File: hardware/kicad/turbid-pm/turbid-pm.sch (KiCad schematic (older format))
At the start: 12 parts, among them J1 Raspbery Pi, J2 PMS 7003, J3 Turbidity sensor, J4 Temp sensor A, J5 Temp sensor B

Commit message: new firmware and docs
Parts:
- removed J5: Temp sensor B, Connector_PinSocket_2.54mm:PinSocket_1x03_P2.54mm_Vertical, symbol Connector:Conn_01x03_Female
- removed R5: 4.7K, Resistor_THT:R_Axial_DIN0207_L6.3mm_D2.5mm_P10.16mm_Horizontal, symbol Device:R
- J4: value Temp sensor A -> Temp sensor
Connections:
- wire segments 30 -> 23
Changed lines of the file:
@@
 P 3450 3350
 F 0 "J4" H 3400 3150 50  0000 C CNN
-F 1 "Temp sensor A" V 3500 3400 50  0000 C CNN
+F 1 "Temp sensor" V 3500 3400 50  0000 C CNN
 F 2 "Connector_PinSocket_2.54mm:PinSocket_1x03_P2.54mm_Vertical" H 3450 3350 50  0001 C CNN
 F 3 "~" H 3450 3350 50  0001 C CNN
@@
 	1    0    0    -1
 $EndComp
-$Comp
-L Connector:Conn_01x03_Female J5
-U 1 1 5EAC2BEB
-P 4250 3350
-F 0 "J5" H 4200 3150 50  0000 C CNN
-F 1 "Temp sensor B" V 4300 3350 50  0000 C CNN
-F 2 "Connector_PinSocket_2.54mm:PinSocket_1x03_P2.54mm_Vertical" H 4250 3350 50  0001 C CNN
-F 3 "~" H 4250 3350 50  0001 C CNN
-	1    4250 3350
-	-1   0    0    1
-$EndComp
-$Comp
-L power:+5V #PWR0113
-U 1 1 5EAC2BF5
-P 4650 3450
-F 0 "#PWR0113" H 4650 3300 50  0001 C CNN
-F 1 "+5V" V 4665 3578 50  0000 L CNN
-F 2 "" H 4650 3450 50  0001 C CNN
-F 3 "" H 4650 3450 50  0001 C CNN
-	1    4650 3450
-	-1   0    0    1
-$EndComp
-$Comp
-L power:Earth #PWR0114
-U 1 1 5EAC2C01
-P 4450 3450
-F 0 "#PWR0114" H 4450 3200 50  0001 C CNN
-F 1 "Earth" H 4450 3300 50  0001 C CNN
-F 2 "" H 4450 3450 50  0001 C CNN
-F 3 "~" H 4450 3450 50  0001 C CNN
-	1    4450 3450
-	1    0    0    -1
-$EndComp
 Wire Wire Line
 	3950 3050 4800 3050
-Wire Wire Line
-	4800 3150 4650 3150
 $Comp
 L Device:R R4
@@
 $EndComp
 Connection ~ 3950 3250
-$Comp
-L Device:R R5
-U 1 1 5EAD38D1
-P 4650 3300
-F 0 "R5" H 4720 3346 50  0000 L CNN
-F 1 "4.7K" V 4650 3200 50  0000 L CNN
-F 2 "Resistor_THT:R_Axial_DIN0207_L6.3mm_D2.5mm_P10.16mm_Horizontal" V 4580 3300 50  0001 C CNN
-F 3 "~" H 4650 3300 50  0001 C CNN
-	1    4650 3300
-	1    0    0    -1
-$EndComp
-Connection ~ 4650 3150
-Wire Wire Line
-	4450 3350 4550 3350
-Wire Wire Line
-	4550 3350 4550 3450
-Wire Wire Line
-	4550 3450 4650 3450
-Connection ~ 4650 3450
 Wire Wire Line
 	3650 3350 3800 3350
@@
 	3800 3550 3950 3550
 Connection ~ 3950 3550
-Wire Wire Line
-	4450 3250 4550 3250
-Wire Wire Line
-	4550 3250 4550 3150
-Wire Wire Line
-	4550 3150 4650 3150
 $EndSCHEMATC

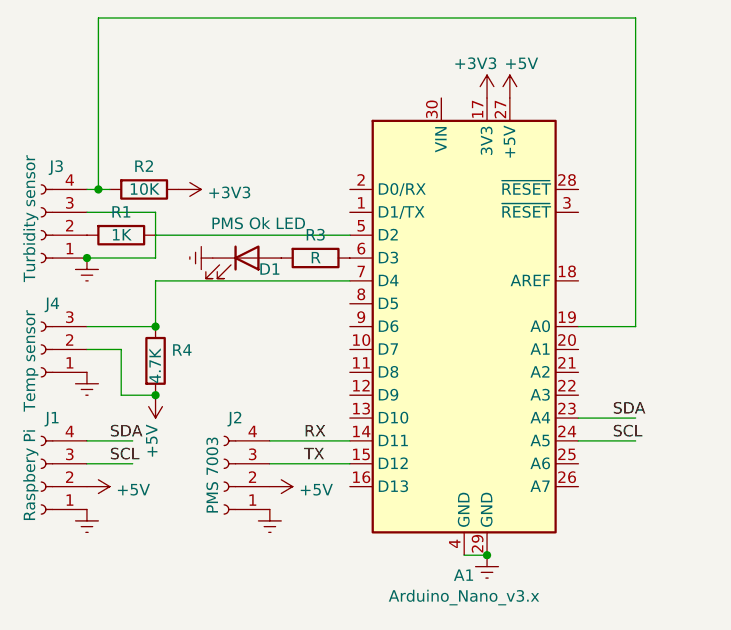
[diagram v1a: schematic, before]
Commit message: adding final action bits
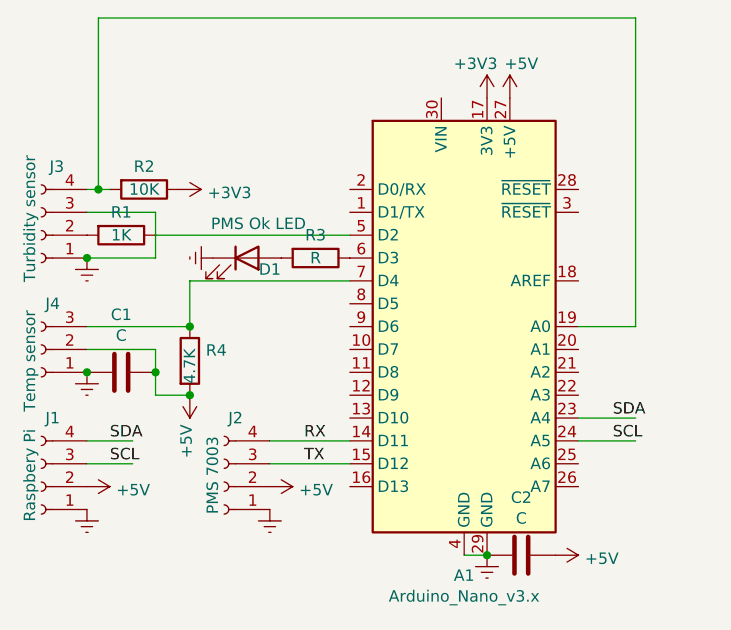
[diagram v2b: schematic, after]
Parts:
- added C1, C2: C, Capacitor_THT:C_Axial_L5.1mm_D3.1mm_P7.50mm_Horizontal, symbol Device:C
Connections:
- wire segments 23 -> 24
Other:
- moved on the sheet: R4
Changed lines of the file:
@@
 L power:+5V #PWR0110
 U 1 1 5EAA9807
-P 3950 3550
-F 0 "#PWR0110" H 3950 3400 50  0001 C CNN
-F 1 "+5V" V 3965 3678 50  0000 L CNN
-F 2 "" H 3950 3550 50  0001 C CNN
-F 3 "" H 3950 3550 50  0001 C CNN
-	1    3950 3550
+P 4100 3550
+F 0 "#PWR0110" H 4100 3400 50  0001 C CNN
+F 1 "+5V" V 4115 3678 50  0000 L CNN
+F 2 "" H 4100 3550 50  0001 C CNN
+F 3 "" H 4100 3550 50  0001 C CNN
+	1    4100 3550
 	-1   0    0    1
 $EndComp
-Wire Wire Line
-	3950 3050 3950 3250
-Wire Wire Line
-	3950 3250 3650 3250
 $Comp
 L power:Earth #PWR0112
@@
 	1    0    0    -1
 $EndComp
-Wire Wire Line
-	3950 3050 4800 3050
 $Comp
 L Device:R R4
 U 1 1 5EAD302D
-P 3950 3400
-F 0 "R4" H 4020 3446 50  0000 L CNN
-F 1 "4.7K" V 3950 3300 50  0000 L CNN
-F 2 "Resistor_THT:R_Axial_DIN0207_L6.3mm_D2.5mm_P10.16mm_Horizontal" V 3880 3400 50  0001 C CNN
-F 3 "~" H 3950 3400 50  0001 C CNN
-	1    3950 3400
+P 4100 3400
+F 0 "R4" H 4170 3446 50  0000 L CNN
+F 1 "4.7K" V 4100 3300 50  0000 L CNN
+F 2 "Resistor_THT:R_Axial_DIN0207_L6.3mm_D2.5mm_P10.16mm_Horizontal" V 4030 3400 50  0001 C CNN
+F 3 "~" H 4100 3400 50  0001 C CNN
+	1    4100 3400
 	1    0    0    -1
 $EndComp
-Connection ~ 3950 3250
+$Comp
+L Device:C C1
+U 1 1 5F2ACADB
+P 3800 3450
+F 0 "C1" V 3548 3450 50  0000 C CNN
+F 1 "C" V 3639 3450 50  0000 C CNN
+F 2 "Capacitor_THT:C_Axial_L5.1mm_D3.1mm_P7.50mm_Horizontal" H 3838 3300 50  0001 C CNN
+F 3 "~" H 3800 3450 50  0001 C CNN
+	1    3800 3450
+	0    1    1    0
+$EndComp
+Connection ~ 3650 3450
 Wire Wire Line
-	3650 3350 3800 3350
+	3950 3450 3950 3350
 Wire Wire Line
-	3800 3350 3800 3550
+	3650 3350 3950 3350
 Wire Wire Line
-	3800 3550 3950 3550
-Connection ~ 3950 3550
+	3650 3250 4100 3250
+Wire Wire Line
+	4800 3050 4100 3050
+Wire Wire Line
+	4100 3050 4100 3250
+Connection ~ 4100 3250
+Wire Wire Line
+	3950 3450 3950 3550
+Wire Wire Line
+	3950 3550 4100 3550
+Connection ~ 3950 3450
+Connection ~ 4100 3550
+$Comp
+L Device:C C2
+U 1 1 5F2C765E
+P 5550 4250
+F 0 "C2" V 5298 4250 50  0000 C CNN
+F 1 "C" V 5389 4250 50  0000 C CNN
+F 2 "Capacitor_THT:C_Axial_L5.1mm_D3.1mm_P7.50mm_Horizontal" H 5588 4100 50  0001 C CNN
+F 3 "~" H 5550 4250 50  0001 C CNN
+	1    5550 4250
+	0    1    1    0
+$EndComp
+$Comp
+L power:+5V #PWR0113
+U 1 1 5F2C81AE
+P 5700 4250
+F 0 "#PWR0113" H 5700 4100 50  0001 C CNN
+F 1 "+5V" V 5715 4378 50  0000 L CNN
+F 2 "" H 5700 4250 50  0001 C CNN
+F 3 "" H 5700 4250 50  0001 C CNN
+	1    5700 4250
+	0    1    1    0
+$EndComp
 $EndSCHEMATC

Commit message: clearing up missing files
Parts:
- C1, C2: value C -> 100nF
- D1: value PMS Ok LED -> Indicator LED
- R3: value R -> 100R
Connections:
- net labels added: Turbidity
- wire segments 24 -> 26
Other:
- moved on the sheet: C2, J1
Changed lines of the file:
@@
 U 1 1 5E9EAFE2
 P 5300 3250
-F 0 "A1" H 5300 2161 50  0000 C CNN
-F 1 "Arduino_Nano_v3.x" H 5300 2070 50  0000 C CNN
+F 0 "A1" H 4850 2200 50  0000 C CNN
+F 1 "Arduino_Nano_v3.x" H 4850 2300 50  0000 C CNN
 F 2 "Module:Arduino_Nano" H 5300 3250 50  0001 C CIN
 F 3 "http://www.mouser.com/pdfdocs/Gravitech_Arduino_Nano3_0.pdf" H 5300 3250 50  0001 C CNN
@@
 P 3450 2850
 F 0 "J3" H 3350 2550 50  0000 L CNN
-F 1 "Turbidity sensor" V 3500 2500 50  0000 L CNN
+F 1 "Turbidity sensor" V 3500 2400 50  0000 L CNN
 F 2 "Connector_PinSocket_2.54mm:PinSocket_1x04_P2.54mm_Vertical" H 3450 2850 50  0001 C CNN
 F 3 "~" H 3450 2850 50  0001 C CNN
@@
 	-1   0    0    1
 $EndComp
-Wire Wire Line
-	5300 4250 5400 4250
 $Comp
 L Connector:Conn_01x04_Female J1
 U 1 1 5E9EDD1F
-P 3450 3950
-F 0 "J1" H 3400 3650 50  0000 C CNN
-F 1 "Raspbery Pi" V 3500 3900 50  0000 C CNN
-F 2 "Connector_PinSocket_2.54mm:PinSocket_1x04_P2.54mm_Vertical" H 3450 3950 50  0001 C CNN
-F 3 "~" H 3450 3950 50  0001 C CNN
-	1    3450 3950
+P 3450 4050
+F 0 "J1" H 3400 3750 50  0000 C CNN
+F 1 "Raspbery Pi" V 3500 4000 50  0000 C CNN
+F 2 "Connector_PinSocket_2.54mm:PinSocket_1x04_P2.54mm_Vertical" H 3450 4050 50  0001 C CNN
+F 3 "~" H 3450 4050 50  0001 C CNN
+	1    3450 4050
 	-1   0    0    1
 $EndComp
@@
 	-1   0    0    1
 $EndComp
+Text Label 3750 3950 0    50   ~ 0
+SCL
 Text Label 3750 3850 0    50   ~ 0
-SCL
-Text Label 3750 3750 0    50   ~ 0
 SDA
 Wire Wire Line
-	3850 3850 3650 3850
+	3850 3950 3650 3950
 $Comp
 L power:Earth #PWR0101
 U 1 1 5EA16092
-P 5400 4250
-F 0 "#PWR0101" H 5400 4000 50  0001 C CNN
-F 1 "Earth" H 5400 4100 50  0001 C CNN
-F 2 "" H 5400 4250 50  0001 C CNN
-F 3 "~" H 5400 4250 50  0001 C CNN
-	1    5400 4250
-	1    0    0    -1
-$EndComp
-Connection ~ 5400 4250
+P 5400 4400
+F 0 "#PWR0101" H 5400 4150 50  0001 C CNN
+F 1 "Earth" H 5400 4250 50  0001 C CNN
+F 2 "" H 5400 4400 50  0001 C CNN
+F 3 "~" H 5400 4400 50  0001 C CNN
+	1    5400 4400
+	1    0    0    -1
+$EndComp
 $Comp
 L power:Earth #PWR0102
@@
 L power:Earth #PWR0103
 U 1 1 5EA17921
-P 3650 4050
-F 0 "#PWR0103" H 3650 3800 50  0001 C CNN
-F 1 "Earth" H 3650 3900 50  0001 C CNN
-F 2 "" H 3650 4050 50  0001 C CNN
-F 3 "~" H 3650 4050 50  0001 C CNN
-	1    3650 4050
+P 3650 4150
+F 0 "#PWR0103" H 3650 3900 50  0001 C CNN
+F 1 "Earth" H 3650 4000 50  0001 C CNN
+F 2 "" H 3650 4150 50  0001 C CNN
+F 3 "~" H 3650 4150 50  0001 C CNN
+	1    3650 4150
 	1    0    0    -1
 $EndComp
@@
 L power:+5V #PWR0106
 U 1 1 5EA24348
-P 3650 3950
-F 0 "#PWR0106" H 3650 3800 50  0001 C CNN
-F 1 "+5V" V 3665 4078 50  0000 L CNN
-F 2 "" H 3650 3950 50  0001 C CNN
-F 3 "" H 3650 3950 50  0001 C CNN
-	1    3650 3950
+P 3650 4050
+F 0 "#PWR0106" H 3650 3900 50  0001 C CNN
+F 1 "+5V" V 3665 4178 50  0000 L CNN
+F 2 "" H 3650 4050 50  0001 C CNN
+F 3 "" H 3650 4050 50  0001 C CNN
+	1    3650 4050
 	0    1    1    0
 $EndComp
@@
 SCL
 Wire Wire Line
-	3650 3750 3850 3750
+	3650 3850 3850 3850
 Wire Wire Line
 	4450 3750 4800 3750
@@
 	0    1    1    0
 $EndComp
-Wire Wire Line
-	3650 2650 3700 2650
-Connection ~ 3700 2650
-Wire Wire Line
-	3700 2650 3750 2650
 $Comp
 L Device:R R1
@@
 Wire Wire Line
 	5800 3250 6050 3250
-Wire Wire Line
-	6050 3250 6050 1900
-Wire Wire Line
-	6050 1900 3700 1900
-Wire Wire Line
-	3700 1900 3700 2650
 $Comp
 L Device:LED D1
@@
 P 4350 2950
 F 0 "D1" H 4450 2900 50  0000 C CNN
-F 1 "PMS Ok LED" H 4400 3100 50  0000 C CNN
+F 1 "Indicator LED" H 4350 2800 50  0000 C CNN
 F 2 "LED_THT:LED_D3.0mm_Clear" H 4350 2950 50  0001 C CNN
 F 3 "~" H 4350 2950 50  0001 C CNN
@@
 P 4650 2950
 F 0 "R3" V 4550 2950 50  0000 C CNN
-F 1 "R" V 4650 2950 50  0000 C CNN
+F 1 "100R" V 4650 2950 50  0000 C CNN
 F 2 "Resistor_THT:R_Axial_DIN0207_L6.3mm_D2.5mm_P10.16mm_Horizontal" V 4580 2950 50  0001 C CNN
 F 3 "~" H 4650 2950 50  0001 C CNN
@@
 P 3450 3350
 F 0 "J4" H 3400 3150 50  0000 C CNN
-F 1 "Temp sensor" V 3500 3400 50  0000 C CNN
+F 1 "Temp sensor" V 3500 3350 50  0000 C CNN
 F 2 "Connector_PinSocket_2.54mm:PinSocket_1x03_P2.54mm_Vertical" H 3450 3350 50  0001 C CNN
 F 3 "~" H 3450 3350 50  0001 C CNN
@@
 U 1 1 5EAD302D
 P 4100 3400
-F 0 "R4" H 4170 3446 50  0000 L CNN
+F 0 "R4" H 4200 3400 50  0000 L CNN
 F 1 "4.7K" V 4100 3300 50  0000 L CNN
 F 2 "Resistor_THT:R_Axial_DIN0207_L6.3mm_D2.5mm_P10.16mm_Horizontal" V 4030 3400 50  0001 C CNN
@@
 U 1 1 5F2ACADB
 P 3800 3450
-F 0 "C1" V 3548 3450 50  0000 C CNN
-F 1 "C" V 3639 3450 50  0000 C CNN
+F 0 "C1" V 3950 3450 50  0000 C CNN
+F 1 "100nF" V 4050 3450 50  0000 C CNN
 F 2 "Capacitor_THT:C_Axial_L5.1mm_D3.1mm_P7.50mm_Horizontal" H 3838 3300 50  0001 C CNN
 F 3 "~" H 3800 3450 50  0001 C CNN
@@
 Wire Wire Line
 	3650 3250 4100 3250
-Wire Wire Line
-	4800 3050 4100 3050
-Wire Wire Line
-	4100 3050 4100 3250
 Connection ~ 4100 3250
 Wire Wire Line
@@
 L Device:C C2
 U 1 1 5F2C765E
-P 5550 4250
-F 0 "C2" V 5298 4250 50  0000 C CNN
-F 1 "C" V 5389 4250 50  0000 C CNN
-F 2 "Capacitor_THT:C_Axial_L5.1mm_D3.1mm_P7.50mm_Horizontal" H 5588 4100 50  0001 C CNN
-F 3 "~" H 5550 4250 50  0001 C CNN
-	1    5550 4250
+P 5550 4300
+F 0 "C2" V 5500 4400 50  0000 C CNN
+F 1 "100nF" V 5650 4500 50  0000 C CNN
+F 2 "Capacitor_THT:C_Axial_L5.1mm_D3.1mm_P7.50mm_Horizontal" H 5588 4150 50  0001 C CNN
+F 3 "~" H 5550 4300 50  0001 C CNN
+	1    5550 4300
 	0    1    1    0
 $EndComp
@@
 L power:+5V #PWR0113
 U 1 1 5F2C81AE
-P 5700 4250
-F 0 "#PWR0113" H 5700 4100 50  0001 C CNN
-F 1 "+5V" V 5715 4378 50  0000 L CNN
-F 2 "" H 5700 4250 50  0001 C CNN
-F 3 "" H 5700 4250 50  0001 C CNN
-	1    5700 4250
-	0    1    1    0
-$EndComp
+P 5700 4300
+F 0 "#PWR0113" H 5700 4150 50  0001 C CNN
+F 1 "+5V" V 5715 4428 50  0000 L CNN
+F 2 "" H 5700 4300 50  0001 C CNN
+F 3 "" H 5700 4300 50  0001 C CNN
+	1    5700 4300
+	0    1    1    0
+$EndComp
+Wire Wire Line
+	4100 3250 4650 3250
+Text Label 5950 3250 0    50   ~ 0
+Turbidity
+Wire Wire Line
+	5400 4250 5400 4300
+Wire Wire Line
+	5400 4300 5400 4400
+Connection ~ 5400 4300
+Wire Wire Line
+	5300 4250 5300 4300
+Wire Wire Line
+	5300 4300 5400 4300
+Wire Wire Line
+	4650 3050 4650 3250
+Wire Wire Line
+	4650 3050 4800 3050
+Wire Wire Line
+	3650 2650 3700 2650
+Wire Wire Line
+	3700 2650 3700 2450
+Connection ~ 3700 2650
+Wire Wire Line
+	3700 2650 3750 2650
+Text Label 3700 2500 0    50   ~ 0
+Turbidity
 $EndSCHEMATC
